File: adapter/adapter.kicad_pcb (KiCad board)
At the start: 2 copper layers, 93.5 x 50.9 mm, 27 parts, among them J1 DF3A-2P-2DSA, J10 Ribbon, J11 Ribbon, J12 Ribbon, J9 Ribbon, SW1 CAS-120TA, U1 nice_nano, U2 nice_nano

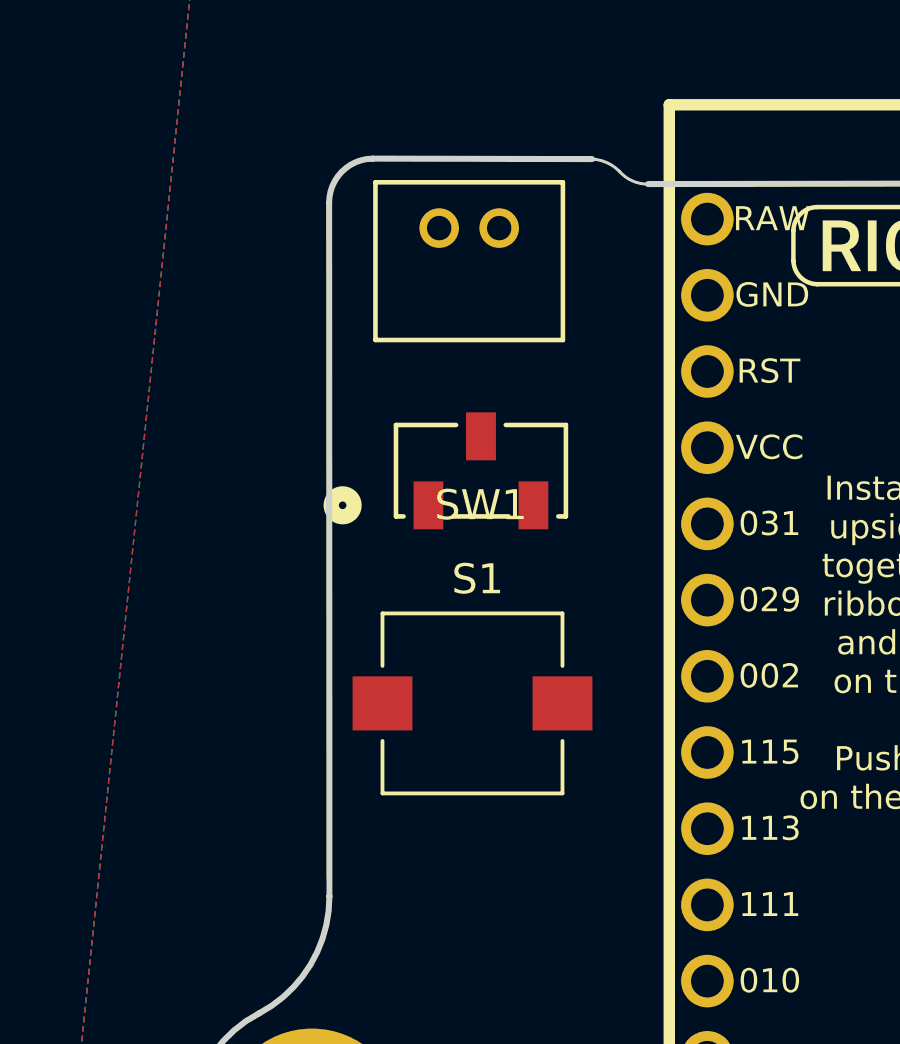
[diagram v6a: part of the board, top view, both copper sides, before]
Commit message: Place all the components onto the pcb
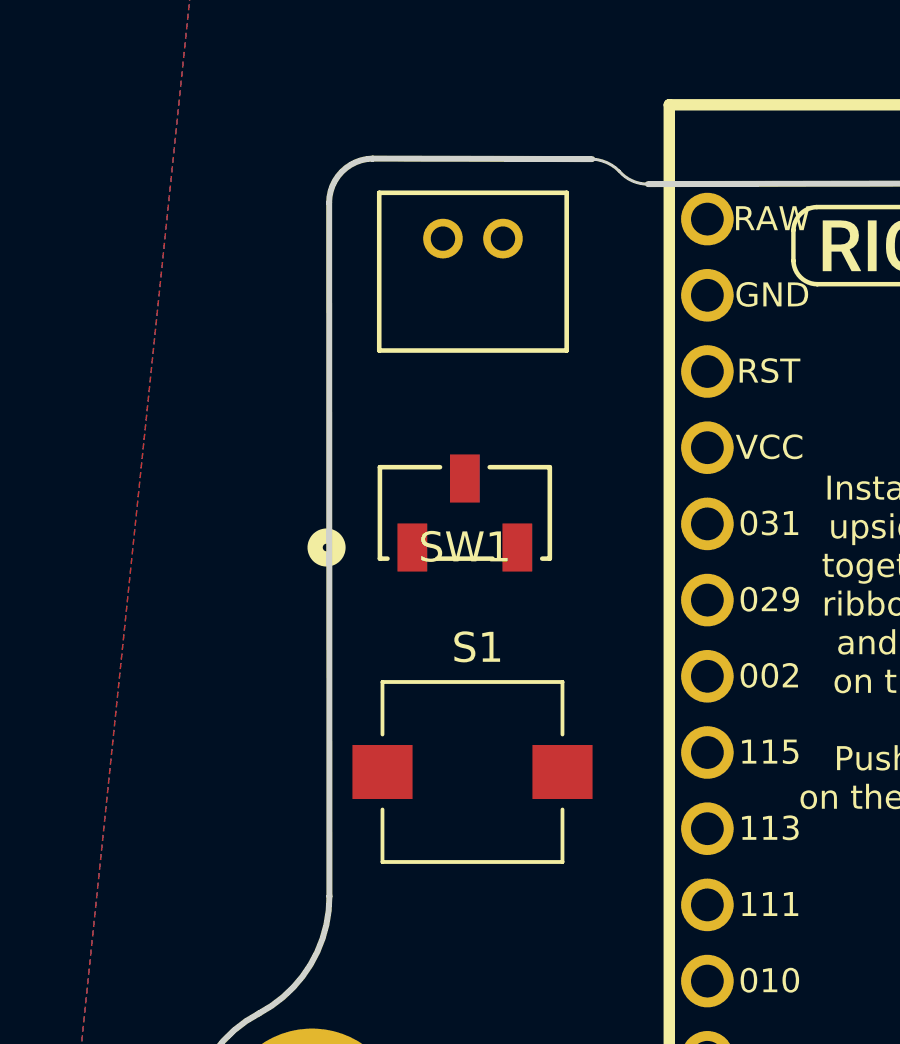
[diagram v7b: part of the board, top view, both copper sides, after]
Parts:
- moved S1 2.29 mm to (118.1, 87.6)
- moved SW1 1.51 mm to (117.9, 79.0)
- moved J1 0.37 mm to (117.1, 69.8)
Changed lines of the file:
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@@
 	(footprint "Library:CAS-120A_NDC"
 		(layer "F.Cu")
-		(at 118.392001 77.587)
+		(at 117.856 78.994)
 		(tags "CAS-120TA ")
 		(property "Reference" "SW1"
@@
 			(fill no)
 			(layer "F.Fab")
-		)
-		(fp_text user "${REFERENCE}"
-			(at 0 1.153 0)
-			(unlocked yes)
-			(layer "F.Fab")
-			(effects
-				(font
-					(size 1 1)
-					(thickness 0.15)
-				)
-			)
 		)
 		(pad "1" smd rect
@@
 		)
 	)
+	(footprint "Library:DF3A_2P_2DSA"
+		(layer "F.Cu")
+		(at 117.125999 69.85)
+		(tags "DF3A-2P-2DSA ")
+		(property "Reference" "J1"
+			(at 1 0 0)
+			(unlocked yes)
+			(layer "F.SilkS")
+			(hide yes)
+			(effects
+				(font
+					(size 1 1)
+					(thickness 0.15)
+				)
+			)
+		)
+		(property "Value" "DF3A-2P-2DSA"
+			(at 1 0 0)
+			(unlocked yes)
+			(layer "F.Fab")
+			(hide yes)
+			(effects
+				(font
+					(size 1 1)
+					(thickness 0.15)
+				)
+			)
+		)
+		(property "Datasheet" "DF3A-2P-2DSA"
+			(at 0 0 0)
+			(layer "F.Fab")
+			(hide yes)
+			(effects
+				(font
+					(size 1.27 1.27)
+					(thickness 0.15)
+				)
+			)
+		)
+		(property "Description" ""
+			(at 0 0 0)
+			(layer "F.Fab")
+			(hide yes)
+			(effects
+				(font
+					(size 1.27 1.27)
+					(thickness 0.15)
+				)
+			)
+		)
+		(property ki_fp_filters "CONN_DF3A-2P-2DSA_HIR")
+		(sheetname "/")
+		(sheetfile "adapter.kicad_sch")
+		(attr through_hole)
+		(fp_line
+			(start -2.1242 -1.527)
+			(end -2.1242 3.7308)
+			(stroke
+				(width 0.1524)
+				(type solid)
+			)
+			(layer "F.SilkS")
+		)
+		(fp_line
+			(start -2.1242 3.7308)
+			(end 4.1242 3.7308)
+			(stroke
+				(width 0.1524)
+				(type solid)
+			)
+			(layer "F.SilkS")
+		)
+		(fp_line
+			(start 4.1242 -1.527)
+			(end -2.1242 -1.527)
+			(stroke
+				(width 0.1524)
+				(type solid)
+			)
+			(layer "F.SilkS")
+		)
+		(fp_line
+			(start 4.1242 3.7308)
+			(end 4.1242 -1.527)
+			(stroke
+				(width 0.1524)
+				(type solid)
+			)
+			(layer "F.SilkS")
+		)
+		(fp_line
+			(start -2.2512 -1.654)
+			(end -2.2512 3.8578)
+			(stroke
+				(width 0.1524)
+				(type solid)
+			)
+			(layer "F.CrtYd")
+		)
+		(fp_line
+			(start -2.2512 3.8578)
+			(end 4.2512 3.8578)
+			(stroke
+				(width 0.1524)
+				(type solid)
+			)
+			(layer "F.CrtYd")
+		)
+		(fp_line
+			(start 4.2512 -1.654)
+			(end -2.2512 -1.654)
+			(stroke
+				(width 0.1524)
+				(type solid)
+			)
+			(layer "F.CrtYd")
+		)
+		(fp_line
+			(start 4.2512 3.8578)
+			(end 4.2512 -1.654)
+			(stroke
+				(width 0.1524)
+				(type solid)
+			)
+			(layer "F.CrtYd")
+		)
+		(fp_line
+			(start -1.9972 -1.4)
+			(end -1.9972 3.6038)
+			(stroke
+				(width 0.0254)
+				(type solid)
+			)
+			(layer "F.Fab")
+		)
+		(fp_line
+			(start -1.9972 3.6038)
+			(end 3.9972 3.6038)
+			(stroke
+				(width 0.0254)
+				(type solid)
+			)
+			(layer "F.Fab")
+		)
+		(fp_line
+			(start 3.9972 -1.4)
+			(end -1.9972 -1.4)
+			(stroke
+				(width 0.0254)
+				(type solid)
+			)
+			(layer "F.Fab")
+		)
+		(fp_line
+			(start 3.9972 3.6038)
+			(end 3.9972 -1.4)
+			(stroke
+				(width 0.0254)
+				(type solid)
+			)
+			(layer "F.Fab")
+		)
+		(pad "1" thru_hole circle
+			(at 0 0)
+			(size 1.3208 1.3208)
+			(drill 0.8128)
+			(layers "*.Cu" "*.Mask")
+			(remove_unused_layers no)
+			(net 23 "GND")
+			(pinfunction "1")
+			(pintype "unspecified")
+		)
+		(pad "2" thru_hole circle
+			(at 2.000001 0)
+			(size 1.3208 1.3208)
+			(drill 0.8128)
+			(layers "*.Cu" "*.Mask")
+			(remove_unused_layers no)
+			(net 32 "BAT+")
+			(pinfunction "2")
+			(pintype "unspecified")
+		)
+		(embedded_fonts no)
+		(model "${KIPRJMOD}/3d/DF3-2P-2DSA.stp"
+			(offset
+				(xyz -0.45 -11.18 1.07)
+			)
+			(scale
+				(xyz 1 1 1)
+			)
+			(rotate
+				(xyz -90 -0 90)
+			)
+		)
+	)
 	(footprint "Library:MountingHole_4mm_Pad_thin"
 		(layer "F.Cu")
@@
 	(footprint "Library:SW_TL9210AF180Q"
 		(layer "F.Cu")
-		(at 118.11 85.344)
+		(at 118.11 87.63)
 		(property "Reference" "S1"
 			(at 0.175 -4.135 0)
@@
 		(embedded_fonts no)
 	)
-	(footprint "Library:DF3A_2P_2DSA"
-		(layer "F.Cu")
-		(at 116.999999 69.5)
-		(tags "DF3A-2P-2DSA ")
-		(property "Reference" "J1"
-			(at 1 0 0)
-			(unlocked yes)
-			(layer "F.SilkS")
-			(hide yes)
-			(effects
-				(font
-					(size 1 1)
-					(thickness 0.15)
-				)
-			)
-		)
-		(property "Value" "DF3A-2P-2DSA"
-			(at 1 0 0)
-			(unlocked yes)
-			(layer "F.Fab")
-			(hide yes)
-			(effects
-				(font
-					(size 1 1)
-					(thickness 0.15)
-				)
-			)
-		)
-		(property "Datasheet" "DF3A-2P-2DSA"
-			(at 0 0 0)
-			(layer "F.Fab")
-			(hide yes)
-			(effects
-				(font
-					(size 1.27 1.27)
-					(thickness 0.15)
-				)
-			)
-		)
-		(property "Description" ""
-			(at 0 0 0)
-			(layer "F.Fab")
-			(hide yes)
-			(effects
-				(font
-					(size 1.27 1.27)
-					(thickness 0.15)
-				)
-			)
-		)
-		(property ki_fp_filters "CONN_DF3A-2P-2DSA_HIR")
-		(sheetname "/")
-		(sheetfile "adapter.kicad_sch")
-		(attr through_hole)
-		(fp_line
-			(start -2.1242 -1.527)
-			(end -2.1242 3.7308)
-			(stroke
-				(width 0.1524)
-				(type solid)
-			)
-			(layer "F.SilkS")
-		)
-		(fp_line
-			(start -2.1242 3.7308)
-			(end 4.1242 3.7308)
-			(stroke
-				(width 0.1524)
-				(type solid)
-			)
-			(layer "F.SilkS")
-		)
-		(fp_line
-			(start 4.1242 -1.527)
-			(end -2.1242 -1.527)
-			(stroke
-				(width 0.1524)
-				(type solid)
-			)
-			(layer "F.SilkS")
-		)
-		(fp_line
-			(start 4.1242 3.7308)
-			(end 4.1242 -1.527)
-			(stroke
-				(width 0.1524)
-				(type solid)
-			)
-			(layer "F.SilkS")
-		)
-		(fp_line
-			(start -2.2512 -1.654)
-			(end -2.2512 3.8578)
-			(stroke
-				(width 0.1524)
-				(type solid)
-			)
-			(layer "F.CrtYd")
-		)
-		(fp_line
-			(start -2.2512 3.8578)
-			(end 4.2512 3.8578)
-			(stroke
-				(width 0.1524)
-				(type solid)
-			)
-			(layer "F.CrtYd")
-		)
-		(fp_line
-			(start 4.2512 -1.654)
-			(end -2.2512 -1.654)
-			(stroke
-				(width 0.1524)
-				(type solid)
-			)
-			(layer "F.CrtYd")
-		)
-		(fp_line
-			(start 4.2512 3.8578)
-			(end 4.2512 -1.654)
-			(stroke
-				(width 0.1524)
-				(type solid)
-			)
-			(layer "F.CrtYd")
-		)
-		(fp_line
-			(start -1.9972 -1.4)
-			(end -1.9972 3.6038)
-			(stroke
-				(width 0.0254)
-				(type solid)
-			)
-			(layer "F.Fab")
-		)
-		(fp_line
-			(start -1.9972 3.6038)
-			(end 3.9972 3.6038)
-			(stroke
-				(width 0.0254)
-				(type solid)
-			)
-			(layer "F.Fab")
-		)
-		(fp_line
-			(start 3.9972 -1.4)
-			(end -1.9972 -1.4)
-			(stroke
-				(width 0.0254)
-				(type solid)
-			)
-			(layer "F.Fab")
-		)
-		(fp_line
-			(start 3.9972 3.6038)
-			(end 3.9972 -1.4)
-			(stroke
-				(width 0.0254)
-				(type solid)
-			)
-			(layer "F.Fab")
-		)
-		(pad "1" thru_hole circle
-			(at 0 0)
-			(size 1.3208 1.3208)
-			(drill 0.8128)
-			(layers "*.Cu" "*.Mask")
-			(remove_unused_layers no)
-			(net 23 "GND")
-			(pinfunction "1")
-			(pintype "unspecified")
-		)
-		(pad "2" thru_hole circle
-			(at 2.000001 0)
-			(size 1.3208 1.3208)
-			(drill 0.8128)
-			(layers "*.Cu" "*.Mask")
-			(remove_unused_layers no)
-			(net 32 "BAT+")
-			(pinfunction "2")
-			(pintype "unspecified")
-		)
-		(embedded_fonts no)
-		(model "C:/Repos/kbd/skeletyle-wireless/DF3-2P-2DSA.stp"
-			(offset
-				(xyz -0.45 -11.19 1.1)
-			)
-			(scale
-				(xyz 1 1 1)
-			)
-			(rotate
-				(xyz 90 -180 -90)
-			)
-		)
-	)
 	(footprint "kibuzzard-61F01A92"
